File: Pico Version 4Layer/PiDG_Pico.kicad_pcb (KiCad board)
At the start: 4 copper layers, 126 x 126 mm, 80 parts, among them J1 Conn_02x05_Odd_Even, J10 Trig, J11 Laser Enable, J12 Pixel Reset, J14 Pico Socket A, J15 Pico Socket B, J16 Laser En/PWM Trig/GND, J17 USB-C PD in, J2 Conn_02x05_Odd_Even, J3 Conn_02x05_Odd_Even, J4 Conn_02x05_Odd_Even, J5 Conn_02x05_Odd_Even, J6 Conn_02x05_Odd_Even, J7 Laser 1, J8 Laser 2, U1 74LVC1G04, U10 74AHCT1G08, U12 74LVC1G17, U13 UCC27524, U14 CH224K, U15 AP63205WU, U16 LM66100, U17 LT3065EDD, U18 TPS3700DDC, U2 SN74LVC04AD, U3 74LVC1G00, U4 SN74LVC04AD, U5 74LVC1G04, U6 SN74LVC04AD, U7 74AHCT1G08, U8 74AHCT1G08, U9 NCP718xSN180

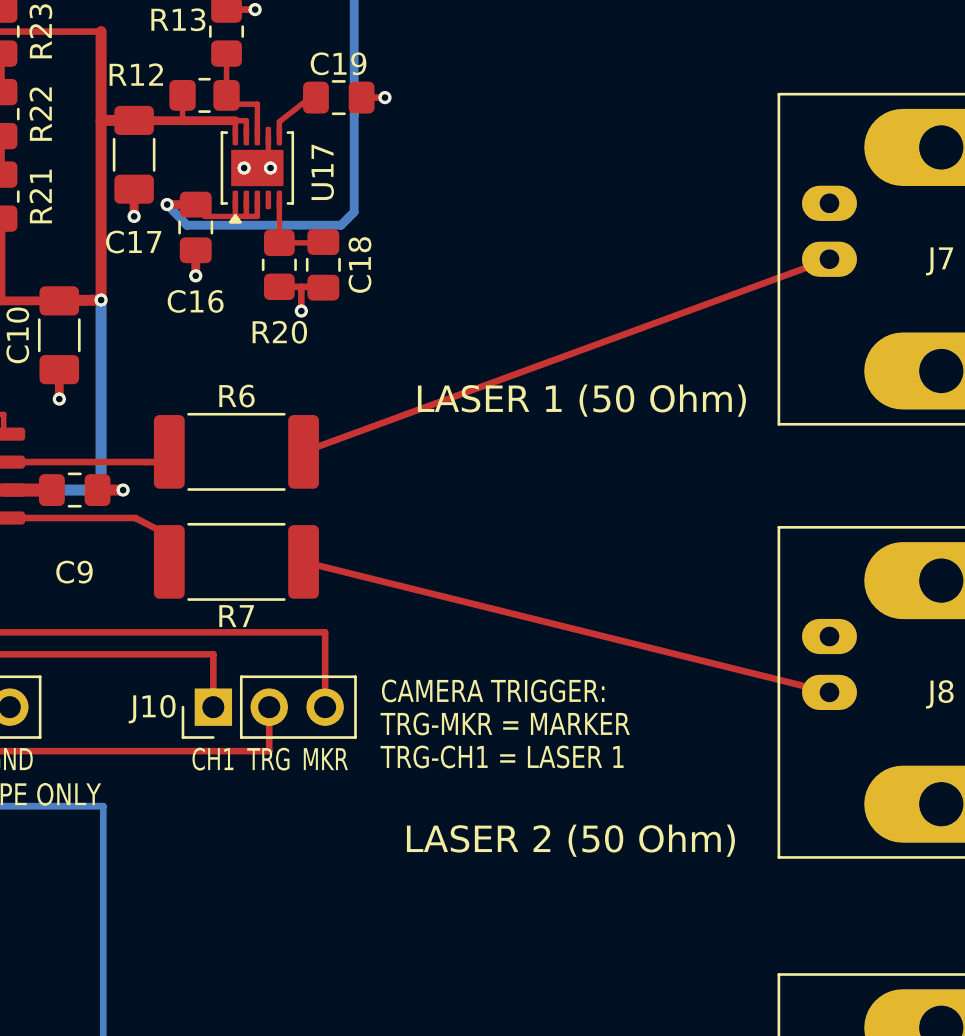
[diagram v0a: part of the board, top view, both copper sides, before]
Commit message: Laser outputs: jumper-selectable 50 ohm / Hi-Z mode per channel
Each laser output gets a 1x3 mode jumper (J18 = Laser 1 / J7, J19 = Laser 2 /
J8), a 47 ohm series resistor (R25/R26) and an 82 ohm shunt to GND (R27/R28),
all 2 W 2512.
- 1-2, 50 ohm mode: the 47 ohm is shorted, so the output is unchanged:
  4.61-5.08 V into the 50 ohm LDP-V input, ~12 V open circuit.
- 2-3, Hi-Z mode: 47 ohm series + 82 ohm shunt give 4.62-5.06 V open circuit
  from a 47.8-49.6 ohm source, i.e. back-terminated, so a long cable into an
  unterminated input has no overshoot (<= 1.02x, 5.14 V max). Into 50 ohm it
  gives 2.3-2.6 V (an LDP-V will not fire).

Board: the blocks sit in the free strip between R6/R7 and the BNCs, with the
series resistor inline on each BNC centre-pin row, orthogonal/45-degree
routing, and channel 2 mirroring channel 1. New silk LASER n OUT / 50Ω / HiZ;
the J10 legend moved below J10. The pre-existing 27-degree CH2_DRIVE_RAW
segment into R7 is now an orthogonal/45-degree jog. Schematic: J7/J8 moved
inside the drawing frame into a new output-mode block with a note.

Checks: ERC 0; DRC 0 violations, 0 unconnected; schematic parity: no real net
conflicts (199 benign warnings, up from 187 for the new pads). Netlist diff
shows only the intended nets. Fab: BOM 43 lines / 82 parts (R25/R26 C5843114,
R27/R28 C7468298, J18/J19 on the C49257 header line); CPLs, gerbers, drill
files and zip regenerated. Docs: README, Hardware.md, JLC_ORDER.md, BOM notes.
Also corrects the stuck-high-into-a-short dissipation of R6/R7 in the docs
(1.6-2.05 W, not 1.9 W; <= 1.4 W at the firmware's maximum duty).

Reviewed by a five-lens adversarial workflow; its confirmed findings are fixed.

Co-Authored-By: Claude Opus 5.5 (1M context) <noreply@anthropic.com>
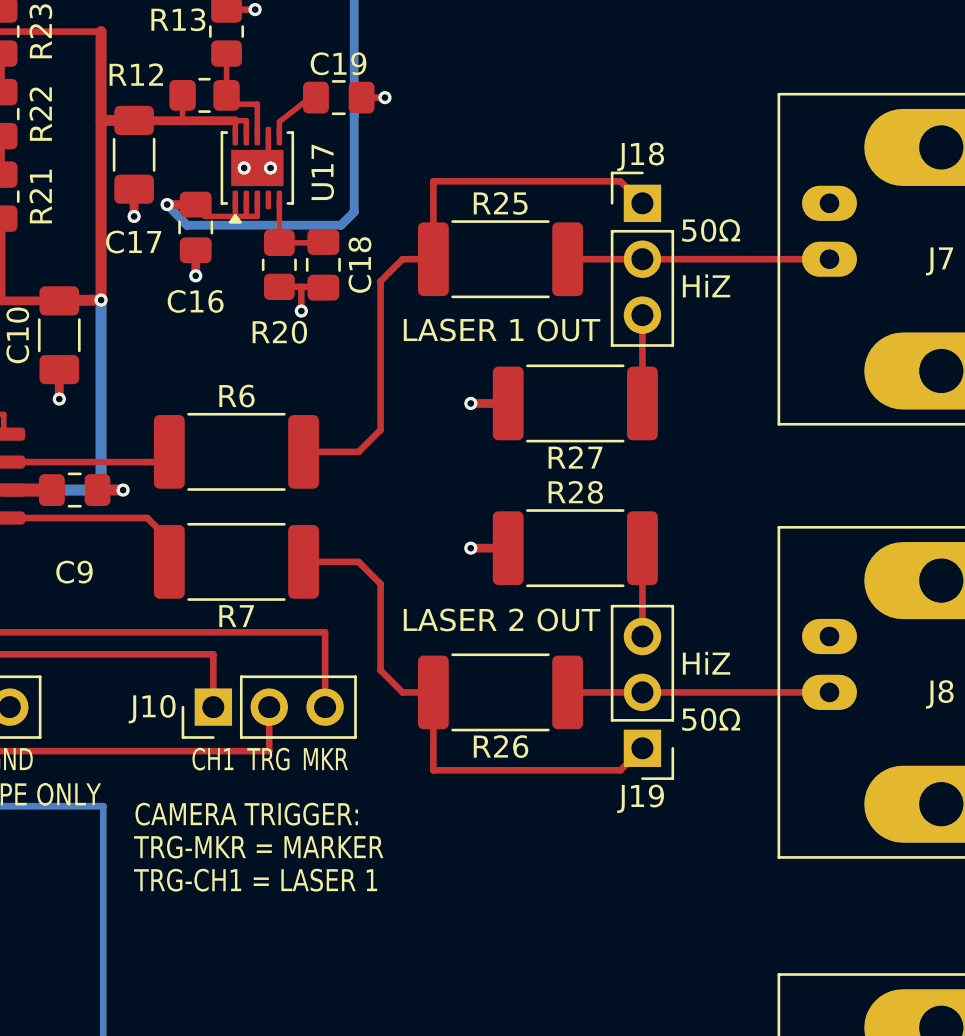
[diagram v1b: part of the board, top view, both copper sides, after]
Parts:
- added J18: Laser 1 mode, Connector_PinHeader_2.54mm:PinHeader_1x03_P2.54mm_Vertical, F.Cu at (236.5, 78.1)
- added J19: Laser 2 mode, Connector_PinHeader_2.54mm:PinHeader_1x03_P2.54mm_Vertical, F.Cu at (236.5, 102.9)
- added R25: 47, Resistor_SMD:R_2512_6332Metric_Pad1.40x3.35mm_HandSolder, F.Cu at (230.1, 80.6)
- added R26: 47, Resistor_SMD:R_2512_6332Metric_Pad1.40x3.35mm_HandSolder, F.Cu at (230.1, 100.3)
- added R27: 82, Resistor_SMD:R_2512_6332Metric_Pad1.40x3.35mm_HandSolder, F.Cu at (233.4, 87.2)
- added R28: 82, Resistor_SMD:R_2512_6332Metric_Pad1.40x3.35mm_HandSolder, F.Cu at (233.4, 93.8)
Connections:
- J7 pad 1: CH1_DRIVE -> CH1_OUT
- J8 pad 1: CH2_DRIVE -> CH2_OUT
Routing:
- net CH2_OUT: track 0.00 -> 11.9 mm
- net CH1_OUT: track 0.00 -> 11.9 mm
- net CH2_TERM: track 0.00 -> 4.02 mm
- net CH1_TERM: track 0.00 -> 4.02 mm
- net GND: track 66.7 -> 70.1 mm, vias 81 -> 83
- net CH1_DRIVE: track 25.5 -> 26.9 mm
- net CH2_DRIVE_RAW: track 7.72 -> 8.93 mm
- net CH2_DRIVE: track 24.6 -> 24.1 mm
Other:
- board text added: "50Ω"
- board text added: "HiZ"
- board text added: "LASER 1 OUT"
- board text added: "LASER 2 OUT"
- board text removed: "LASER 1 (50 Ohm)"
- board text removed: "LASER 2 (50 Ohm)"

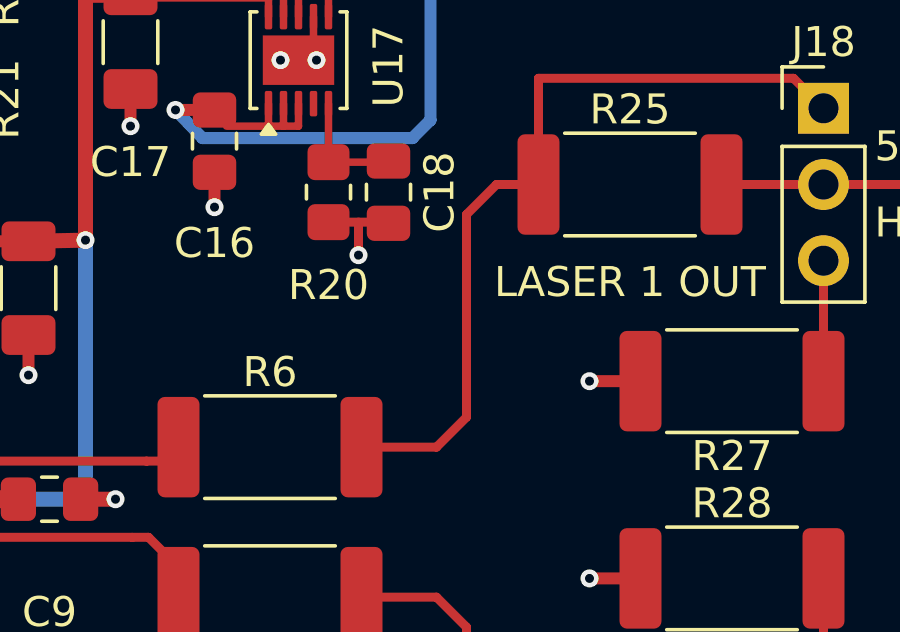
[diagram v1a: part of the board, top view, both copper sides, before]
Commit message: Laser outputs: equalise the CH1 and CH2 path lengths
R6/R7 are not symmetric about the output-mode blocks' mirror line, so CH1 was
1.88 mm longer than CH2 (U13 pad to the 47 ohm resistor). CH1's feed from R6
now takes larger 45-degree corners (riser at x 224.4, upper corner landing on
the R25 pad 1 centre), with no detour: both channels are 19.593 mm from U13
to the series resistor, and every path on to the BNCs is mirrored, so the
lengths match in both modes. DRC 0 / 0 unconnected; gerbers, drill files,
zip and the stored DRC report regenerated; Hardware.md updated.

Co-Authored-By: Claude Opus 5.5 (1M context) <noreply@anthropic.com>
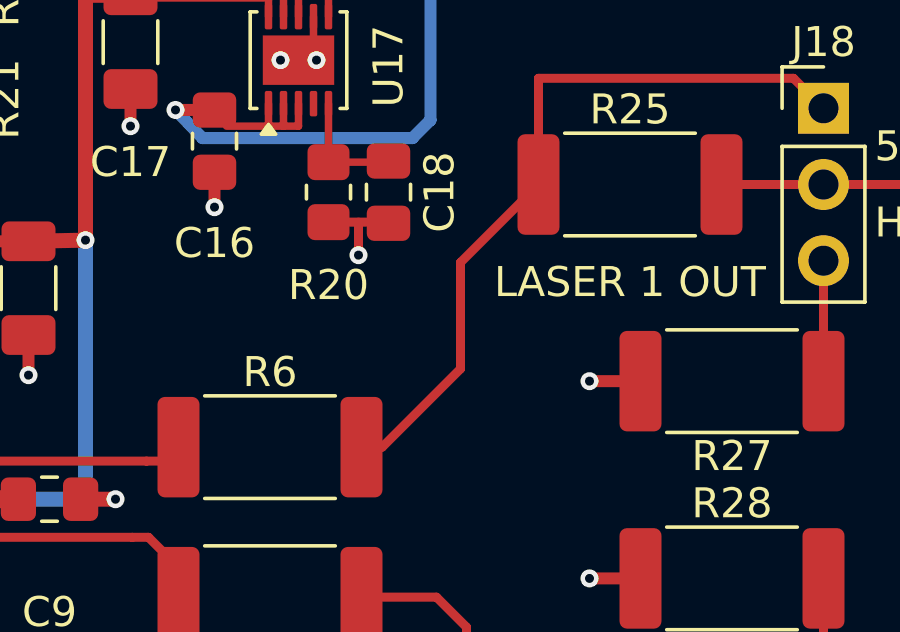
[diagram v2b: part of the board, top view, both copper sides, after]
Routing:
- net CH1_DRIVE: track 26.9 -> 25.1 mm
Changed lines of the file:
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@@
-	)
-	(segment
-		(start 221.1 89.4)
-		(end 223.6 89.4)
-		(width 0.3)
-		(layer "F.Cu")
-		(net "CH1_DRIVE")
 	)
 	(segment
@@
 	)
 	(segment
-		(start 223.6 89.4)
-		(end 224.6 88.4)
+		(start 221.7899 89.4)
+		(end 224.4 86.7899)
 		(width 0.3)
 		(layer "F.Cu")
@@
 	)
 	(segment
-		(start 225.6 80.645)
+		(start 224.4 83.245)
 		(end 227 80.645)
 		(width 0.3)
@@
 	)
 	(segment
-		(start 224.6 81.645)
-		(end 225.6 80.645)
+		(start 224.4 86.7899)
+		(end 224.4 83.245)
 		(width 0.3)
 		(layer "F.Cu")
@@
 	)
 	(segment
-		(start 224.6 88.4)
-		(end 224.6 81.645)
+		(start 221.1 89.4)
+		(end 221.7899 89.4)
 		(width 0.3)
 		(layer "F.Cu")
